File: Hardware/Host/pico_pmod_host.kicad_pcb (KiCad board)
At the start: 2 copper layers, 66 x 43.2 mm, 8 parts, among them J1 Conn_02x15_Odd_Even, J2 Conn_01x02, J3 Conn_01x02, J4 Conn_01x02, J5 Conn_01x03, J7 Conn_01x05, SW1 SW_Push, U1 Pico

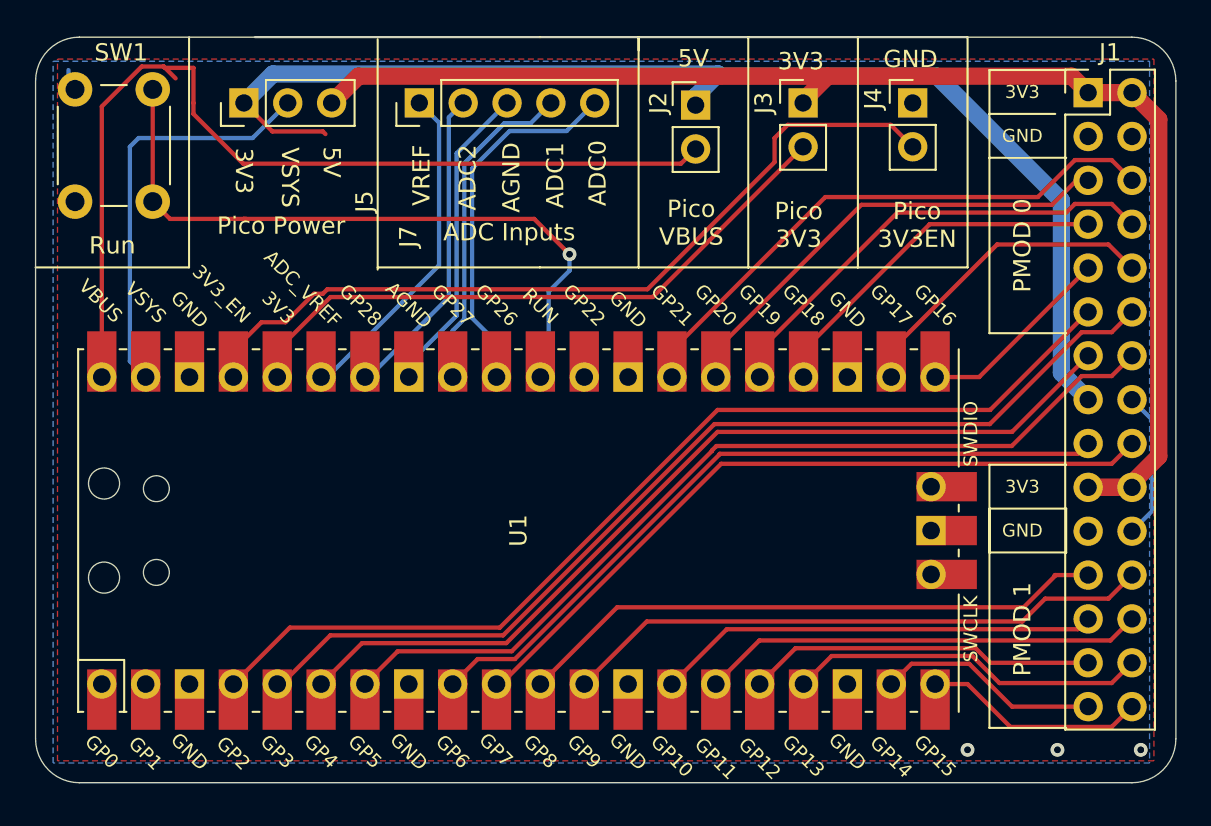
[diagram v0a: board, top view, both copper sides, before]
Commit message: PMOD connector corrected to match schematic
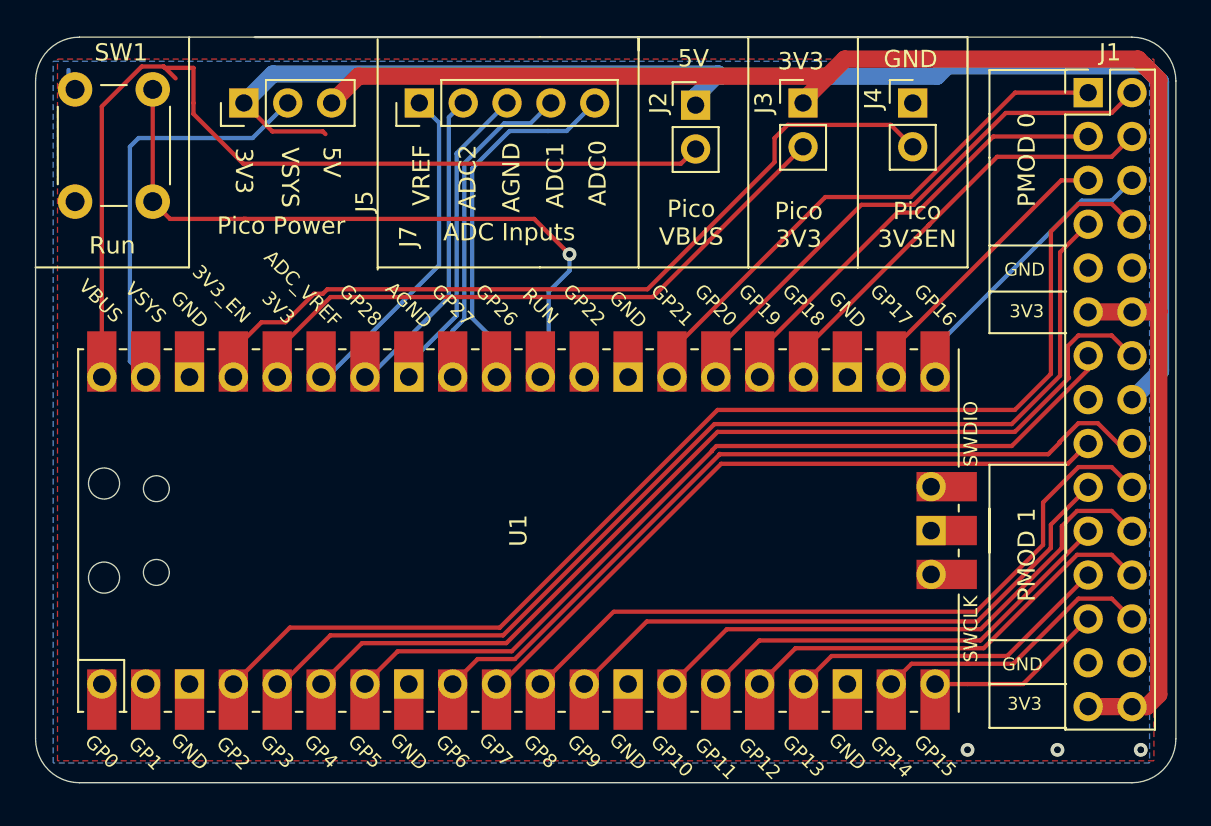
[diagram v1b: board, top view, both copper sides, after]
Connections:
- J1 pad 1: +3V3 -> GPIO_21
- J1 pad 10: GPIO_17 -> GND
- J1 pad 11: GPIO_02 -> +3V3
- J1 pad 12: GPIO_03 -> +3V3
- J1 pad 13: GPIO_04 -> GPIO_05
- J1 pad 14: GPIO_05 -> GPIO_04
- J1 pad 15: +5V -> GND
- J1 pad 16: GND -> +5V
- J1 pad 17: GPIO_06 -> GPIO_07
- J1 pad 18: GPIO_07 -> GPIO_06
- J1 pad 19: +3V3 -> GPIO_09
- J1 pad 2: +3V3 -> GPIO_20
- J1 pad 20: +3V3 -> GPIO_08
- J1 pad 21: GND -> GPIO_11
- J1 pad 22: GND -> GPIO_10
- J1 pad 23: GPIO_08 -> GPIO_13
- J1 pad 24: GPIO_09 -> GPIO_12
- J1 pad 25: GPIO_10 -> GPIO_15
- J1 pad 26: GPIO_11 -> GPIO_14
- J1 pad 27: GPIO_12 -> GND
- J1 pad 28: GPIO_13 -> GND
- J1 pad 29: GPIO_14 -> +3V3
- J1 pad 3: GND -> GPIO_19
- J1 pad 30: GPIO_15 -> +3V3
- J1 pad 4: GND -> GPIO_18
- J1 pad 5: GPIO_20 -> GPIO_17
- J1 pad 6: GPIO_21 -> GPIO_16
- J1 pad 7: GPIO_18 -> GPIO_03
- J1 pad 8: GPIO_19 -> GPIO_02
- J1 pad 9: GPIO_16 -> GND
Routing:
- net GPIO_02: track 58.4 -> 68.9 mm
- net +5V: track 71.1 -> 81.4 mm
- net GND: track 9.87 -> 1.28 mm
- net GPIO_08: track 34.4 -> 41.4 mm
- net GPIO_10: track 25.7 -> 32.0 mm
- net GPIO_16: track 11.5 -> 17.1 mm
- net GPIO_12: track 20.2 -> 25.2 mm
- net GPIO_18: track 21.1 -> 25.8 mm
- net GPIO_04: track 52.3 -> 57.0 mm
- net GPIO_20: track 27.2 -> 31.8 mm
- net GPIO_03: track 58.8 -> 62.5 mm
- net GPIO_14: track 12.9 -> 16.6 mm
- net GPIO_06: track 42.6 -> 46.1 mm
- net GPIO_15: track 12.9 -> 10.4 mm
- net GPIO_05: track 52.3 -> 50.2 mm
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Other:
- board text added: "Raspberry Pi Pico PMod Host @JamesjHorton JJHorton.co.uk"
- board text removed: "Raspberry Pi Pico PMod @JamesjHorton JJHorton.co.uk"
